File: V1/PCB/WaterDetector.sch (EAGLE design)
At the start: 13 parts

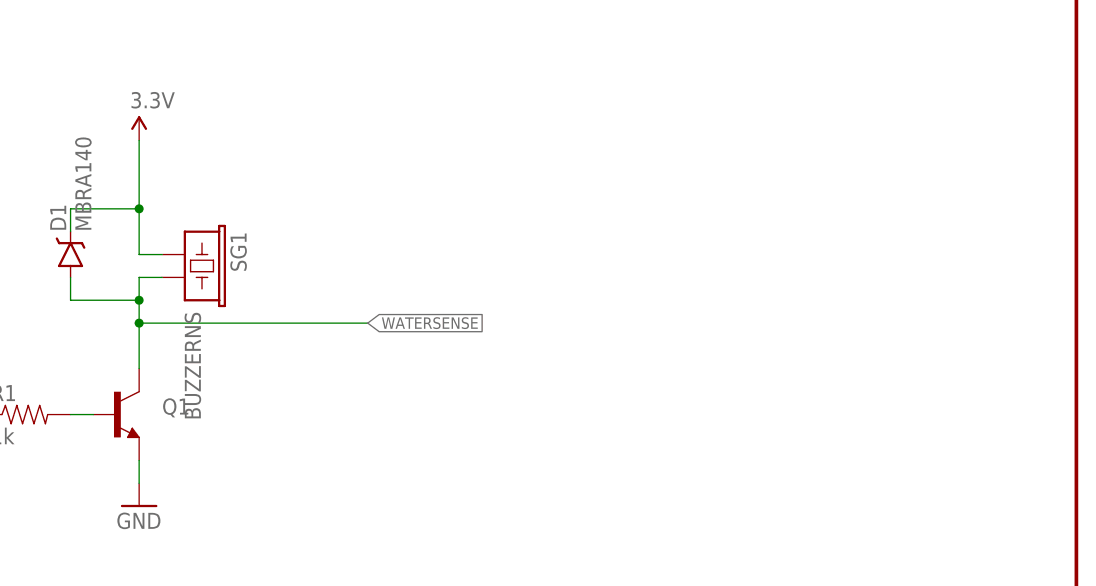
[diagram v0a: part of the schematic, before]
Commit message: Added bodge resistor required to pull LED drive low to prevent LEDs switching on when Photon is in power save mode.
"Printed" eagle files as pdfs.
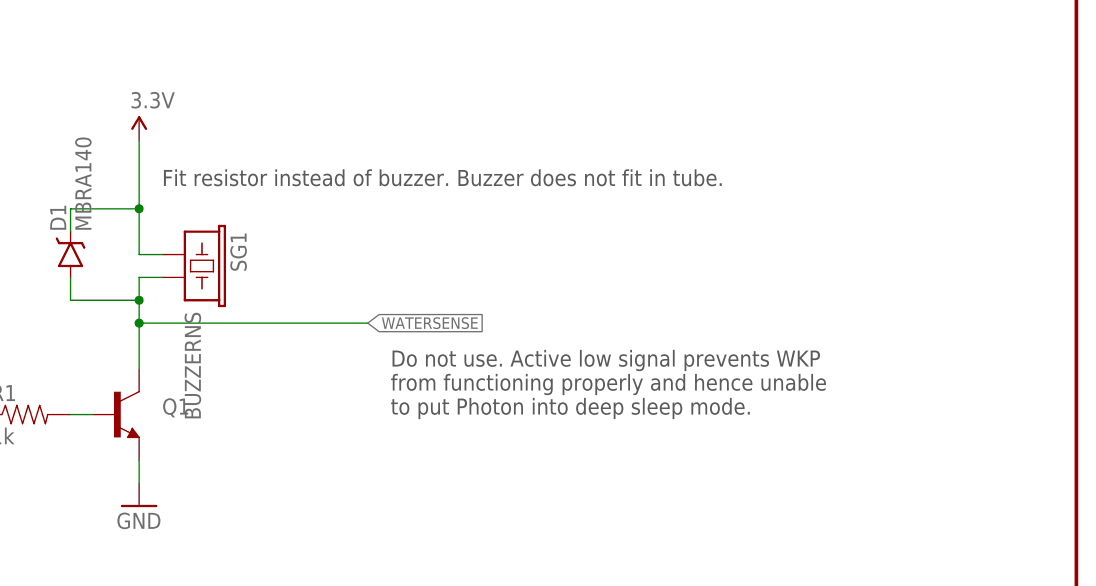
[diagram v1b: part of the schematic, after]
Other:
- note added: "Do not use. Active low signal prevents WKP from functioning properly and hence unable to put Photon into deep sleep mode."
- note added: "Fit resistor instead of buzzer. Buzzer does not fit in tube."
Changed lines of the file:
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@@
 <plain>
 <text x="106.68" y="144.78" size="1.27" layer="97">Batt -VE connected to GND</text>
+<text x="172.72" y="93.98" size="1.778" layer="97">Do not use. Active low signal prevents WKP
+from functioning properly and hence unable
+to put Photon into deep sleep mode.</text>
+<text x="147.32" y="119.38" size="1.778" layer="97">Fit resistor instead of buzzer. Buzzer does not fit in tube.</text>
 </plain>
 <instances>
@@
 </schematic>
 </drawing>
+<compatibility>
+<note version="6.3" minversion="6.2.2" severity="warning">
+Since Version 6.2.2 text objects can contain more than one line,
+which will not be processed correctly with this version.
+</note>
+</compatibility>
 </eagle>
